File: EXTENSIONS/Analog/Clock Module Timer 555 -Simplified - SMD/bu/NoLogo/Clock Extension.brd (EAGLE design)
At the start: 53 x 43 mm, 7 parts

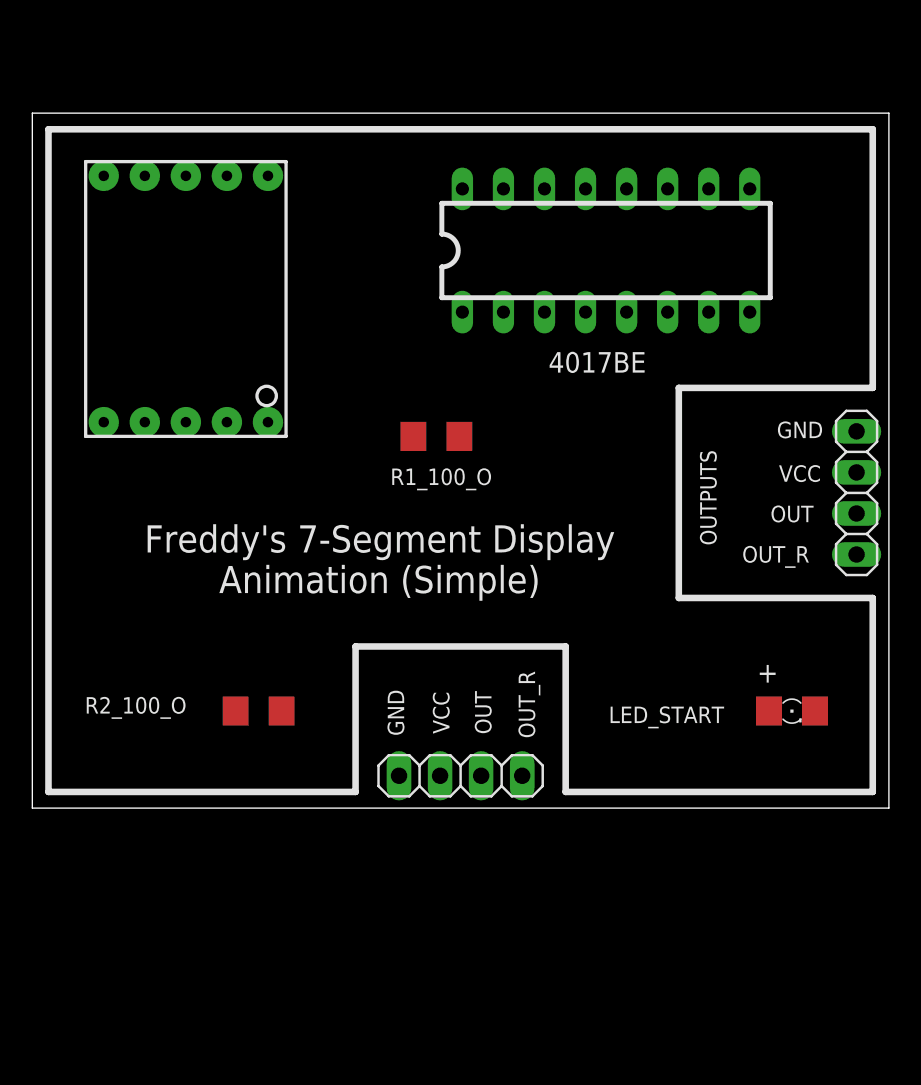
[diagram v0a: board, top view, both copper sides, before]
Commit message: Create new clock module SMD
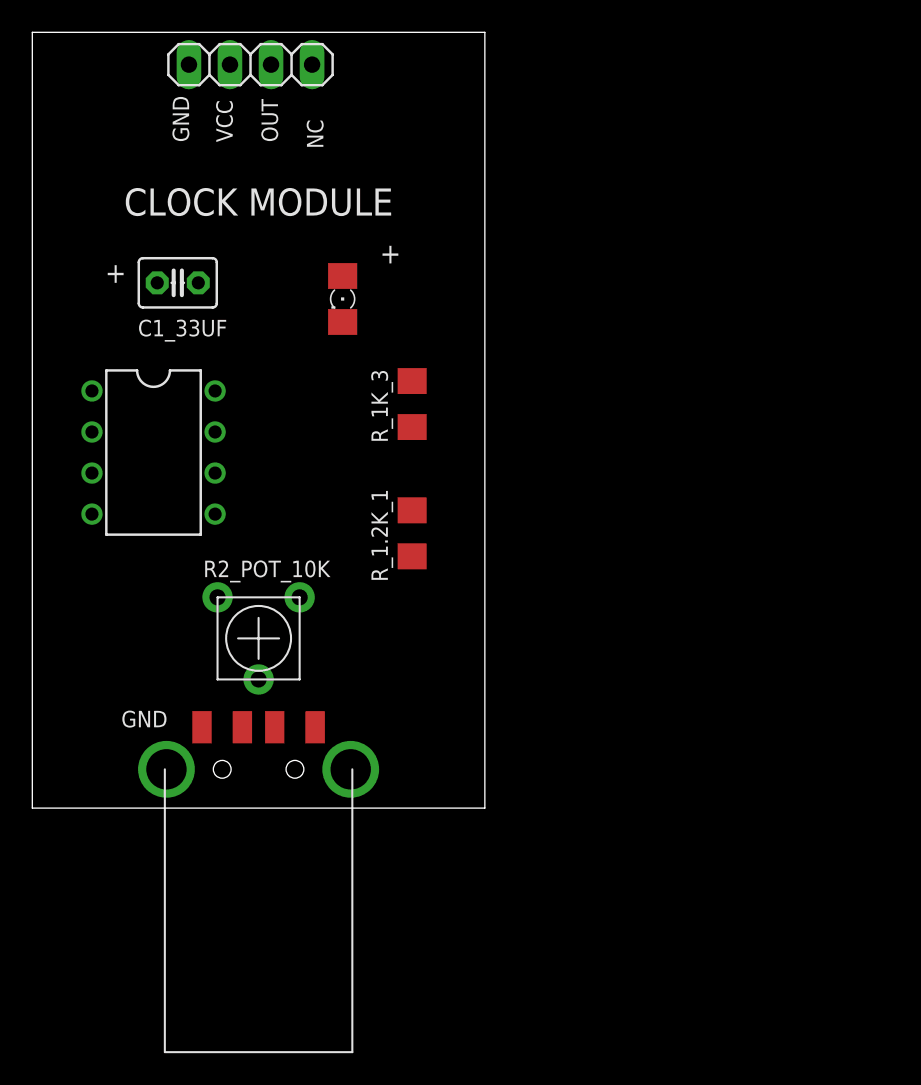
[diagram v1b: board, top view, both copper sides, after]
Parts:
- removed 4017BE: CD4017, SparkFun-DigitalIC:DIL16
- removed JP_CLOCK_IN, OUTPUTS: (no value), pinhead:1X04
- removed LED_START: (no value), adafruit:1206
- removed R1_100_O, R2_100_O: (no value), adafruit:R1206
- removed U$1: 7-SEGMENT-DISPLAYPTH, SparkFun-Displays:7-SEGMENT-DISPLAY
- added C1_33UF: (no value), adafruit:C025-030X050
- added JP1: (no value), pinhead:1X04
- added LED_OUTPUT: (no value), adafruit:1206
- added R2_POT_10K: (no value), SparkFun-Electromechanical:TRIM_POT_PTH
- added R_1.2K_1, R_1K_3: (no value), adafruit:R1206
- added T555_CLOCK: NE555N, linear:DIL08
- added X1: USB-A, adafruit:MOLEX_480371000
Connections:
- removed net N$2: R1_100_O.2, U$1.8
- removed net RESET: 4017BE.15, 4017BE.6
- removed net SEG_A: 4017BE.3, LED_START.A, U$1.7
- removed net SEG_B: 4017BE.2, U$1.6
- removed net SEG_C: 4017BE.4, U$1.4
- removed net SEG_D: 4017BE.7, U$1.2
- removed net SEG_DP: U$1.5
- removed net SEG_E: 4017BE.10, U$1.1
- removed net SEG_F: 4017BE.1, U$1.9
- removed net SEG_G: 4017BE.5, U$1.10
- new net N$5: LED_OUTPUT.C, R_1K_3.2
- new net THRESHOLD: C1_33UF.2, R2_POT_10K.2, T555_CLOCK.2, T555_CLOCK.6
- net GND: now also C1_33UF.1, JP1.1, R_1K_3.1, T555_CLOCK.1, X1.4; no longer 4017BE.13, 4017BE.8, JP_CLOCK_IN.1, OUTPUTS.1, R1_100_O.1, R2_100_O.1
- net N$1: now also R2_POT_10K.3, R_1.2K_1.1, T555_CLOCK.7; no longer LED_START.C, R2_100_O.2
- net TMR555_OUTPUT: now also JP1.3, LED_OUTPUT.A, T555_CLOCK.3; no longer 4017BE.14, JP_CLOCK_IN.3, OUTPUTS.3
- net TMR555_OUTPUT_REVERSE: now also JP1.4; no longer JP_CLOCK_IN.4, OUTPUTS.4
- net VCC: now also JP1.2, R_1.2K_1.2, T555_CLOCK.4, T555_CLOCK.8, X1.1; no longer 4017BE.16, JP_CLOCK_IN.2, OUTPUTS.2
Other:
- board size 53 x 43 mm -> 28 x 48 mm
- board text added: "CLOCK MODULE"
- board text added: "NC"
- board text added: "PCBv3 - 2019.08"
- board text removed: "Freddy's 7-Segment Display Animation (Simple)"
- board text removed: "OUT_R"
- board text removed: "PCBv2 - 2019.12"
- board text removed: "https://bit.ly/36Fu0YN"
- board text removed: "www.FredericTorres.com"
